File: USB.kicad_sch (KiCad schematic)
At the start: 8 parts, among them J11 USB_B_Micro, U8 CP2102N-A02-GQFN24

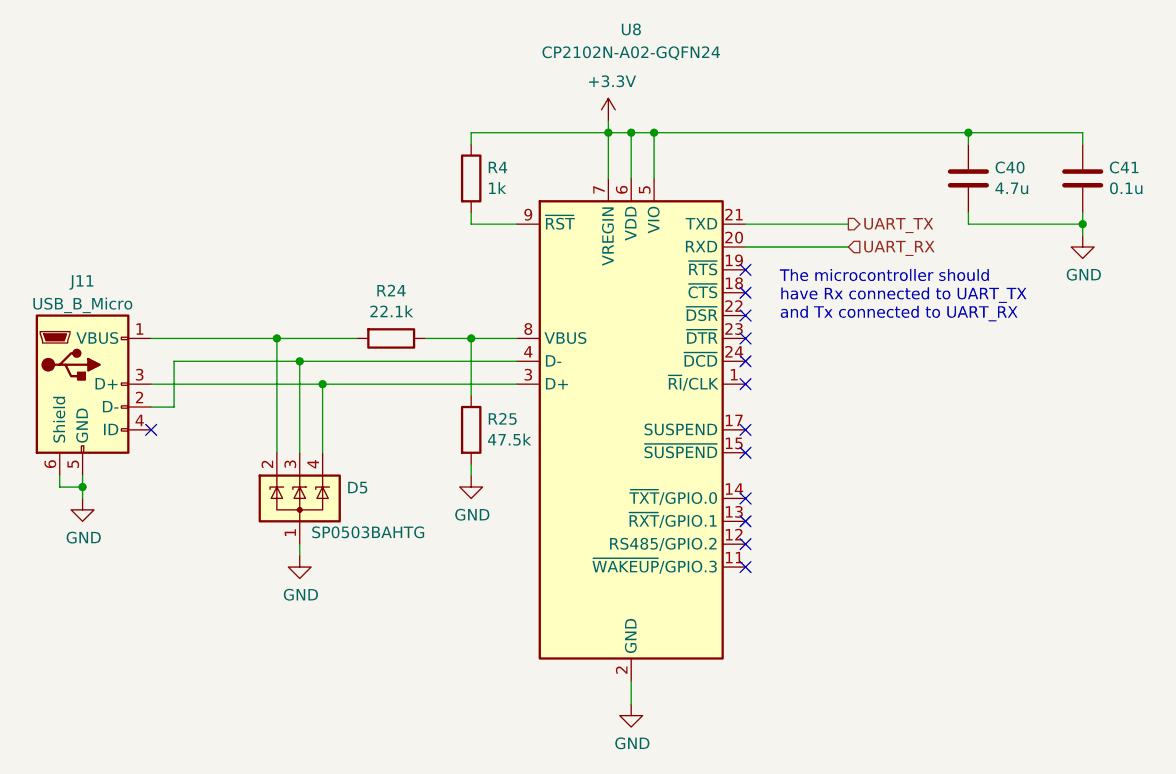
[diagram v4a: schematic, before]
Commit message: inputs routing + fixed models + clock keepouts
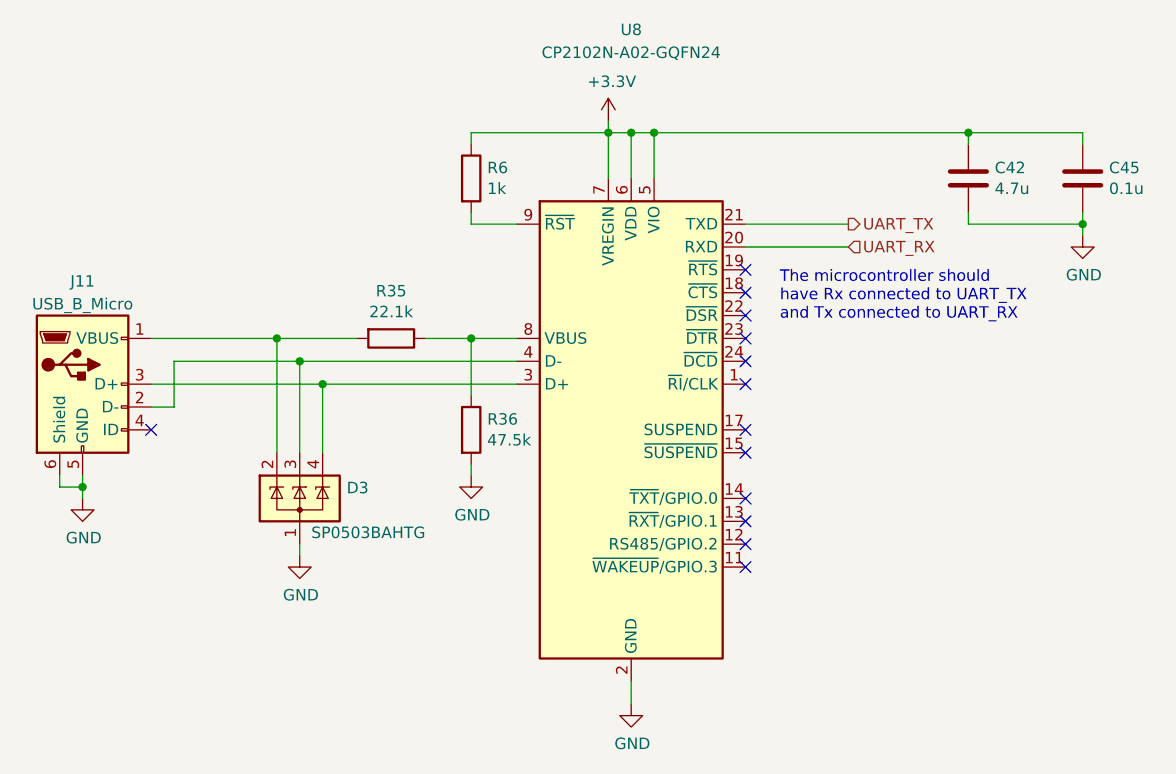
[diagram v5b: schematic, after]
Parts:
- renumbered C40 to C42, C41 to C45, D5 to D3, R24 to R35, R25 to R36, R4 to R6
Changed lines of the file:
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@@
         )
         (path "/7f2a449b-14af-42b3-8d38-5f0f8a5ee7ce/65ccd205-e43e-414f-91f4-e0a7c33b5687"
-          (reference "J6") (unit 1)
+          (reference "J11") (unit 1)
         )
       )
@@
   (symbol (lib_id "Power_Protection:SP0503BAHT") (at 113.03 111.125 0) (unit 1)
     (in_bom yes) (on_board yes) (dnp no)
-    (property "Reference" "D5" (at 118.237 109.9566 0)
+    (property "Reference" "D3" (at 118.237 109.9566 0)
       (effects (font (size 1.27 1.27)) (justify left))
     )
@@
       (project "Telemetry-Primary"
         (path "/7f2a449b-14af-42b3-8d38-5f0f8a5ee7ce/65ccd205-e43e-414f-91f4-e0a7c33b5687"
-          (reference "D5") (unit 1)
+          (reference "D3") (unit 1)
         )
       )
@@
   (symbol (lib_id "Device:R") (at 132.08 103.505 0) (unit 1)
     (in_bom yes) (on_board yes) (dnp no)
-    (property "Reference" "R25" (at 133.858 102.3366 0)
+    (property "Reference" "R36" (at 133.858 102.3366 0)
       (effects (font (size 1.27 1.27)) (justify left))
     )
@@
       (project "Telemetry-Primary"
         (path "/7f2a449b-14af-42b3-8d38-5f0f8a5ee7ce/65ccd205-e43e-414f-91f4-e0a7c33b5687"
-          (reference "R25") (unit 1)
+          (reference "R36") (unit 1)
         )
       )
@@
   (symbol (lib_id "Device:R") (at 123.19 93.345 270) (unit 1)
     (in_bom yes) (on_board yes) (dnp no)
-    (property "Reference" "R24" (at 123.19 88.0872 90)
+    (property "Reference" "R35" (at 123.19 88.0872 90)
       (effects (font (size 1.27 1.27)))
     )
@@
       (project "Telemetry-Primary"
         (path "/7f2a449b-14af-42b3-8d38-5f0f8a5ee7ce/65ccd205-e43e-414f-91f4-e0a7c33b5687"
-          (reference "R24") (unit 1)
+          (reference "R35") (unit 1)
         )
       )
@@
   (symbol (lib_id "Device:R") (at 132.08 75.565 0) (unit 1)
     (in_bom yes) (on_board yes) (dnp no)
-    (property "Reference" "R4" (at 133.858 74.3966 0)
+    (property "Reference" "R6" (at 133.858 74.3966 0)
       (effects (font (size 1.27 1.27)) (justify left))
     )
@@
       (project "Telemetry-Primary"
         (path "/7f2a449b-14af-42b3-8d38-5f0f8a5ee7ce/65ccd205-e43e-414f-91f4-e0a7c33b5687"
-          (reference "R4") (unit 1)
+          (reference "R6") (unit 1)
         )
       )
@@
   (symbol (lib_id "Device:C") (at 187.325 75.565 0) (unit 1)
     (in_bom yes) (on_board yes) (dnp no)
-    (property "Reference" "C40" (at 190.246 74.3966 0)
+    (property "Reference" "C42" (at 190.246 74.3966 0)
       (effects (font (size 1.27 1.27)) (justify left))
     )
@@
       (project "Telemetry-Primary"
         (path "/7f2a449b-14af-42b3-8d38-5f0f8a5ee7ce/65ccd205-e43e-414f-91f4-e0a7c33b5687"
-          (reference "C40") (unit 1)
+          (reference "C42") (unit 1)
         )
       )
@@
   (symbol (lib_id "Device:C") (at 200.025 75.565 0) (unit 1)
     (in_bom yes) (on_board yes) (dnp no)
-    (property "Reference" "C41" (at 202.946 74.3966 0)
+    (property "Reference" "C45" (at 202.946 74.3966 0)
       (effects (font (size 1.27 1.27)) (justify left))
     )
@@
       (project "Telemetry-Primary"
         (path "/7f2a449b-14af-42b3-8d38-5f0f8a5ee7ce/65ccd205-e43e-414f-91f4-e0a7c33b5687"
-          (reference "C41") (unit 1)
-        )
-      )
+          (reference "C45") (unit 1)
+        )
+      )
